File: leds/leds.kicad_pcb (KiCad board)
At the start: 2 copper layers, 230 x 230 mm, 51 parts, among them J101 Conn_02x05_Odd_Even, J102 Conn_02x05_Odd_Even

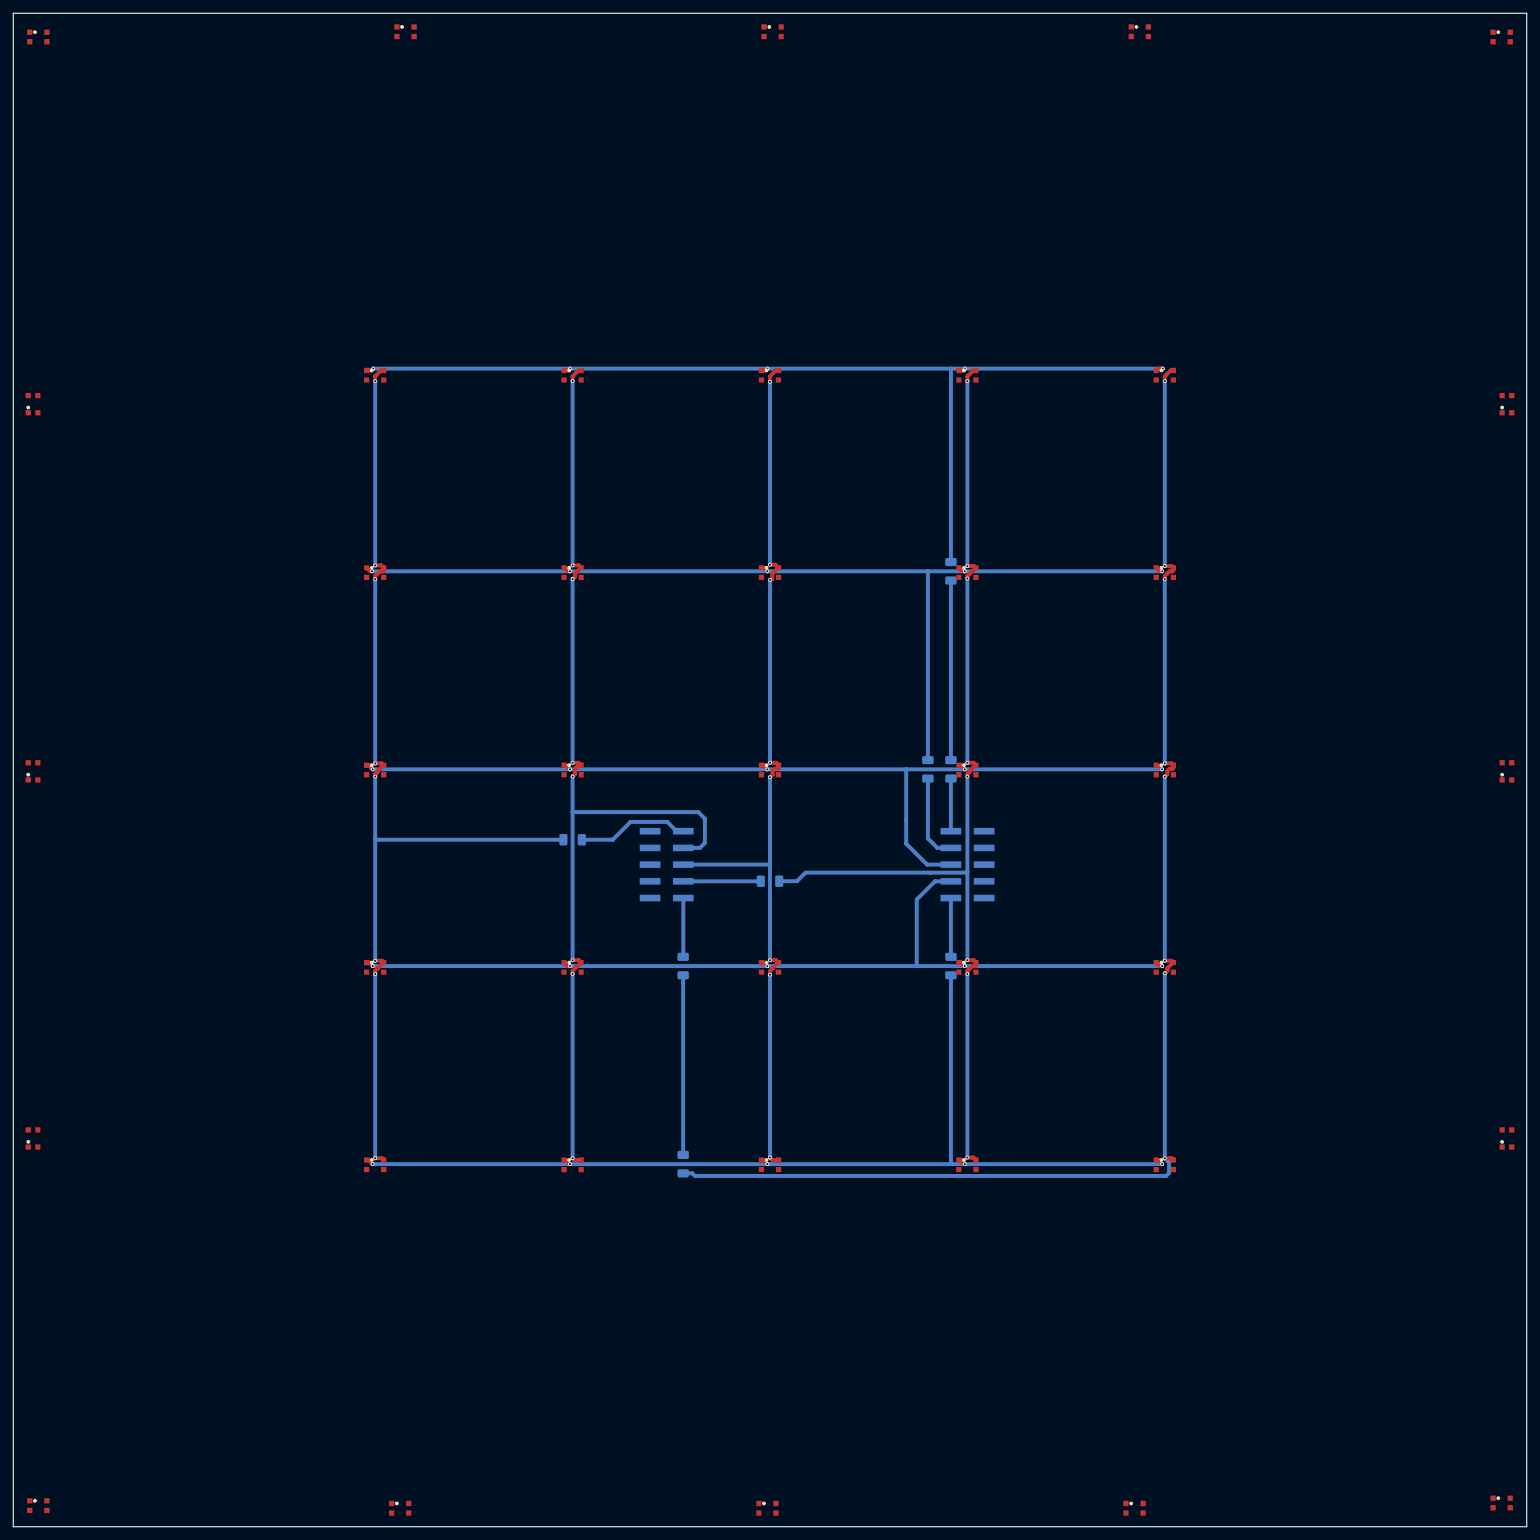
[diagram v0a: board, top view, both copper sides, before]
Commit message: remove unused LEDs, add paste in gerber output
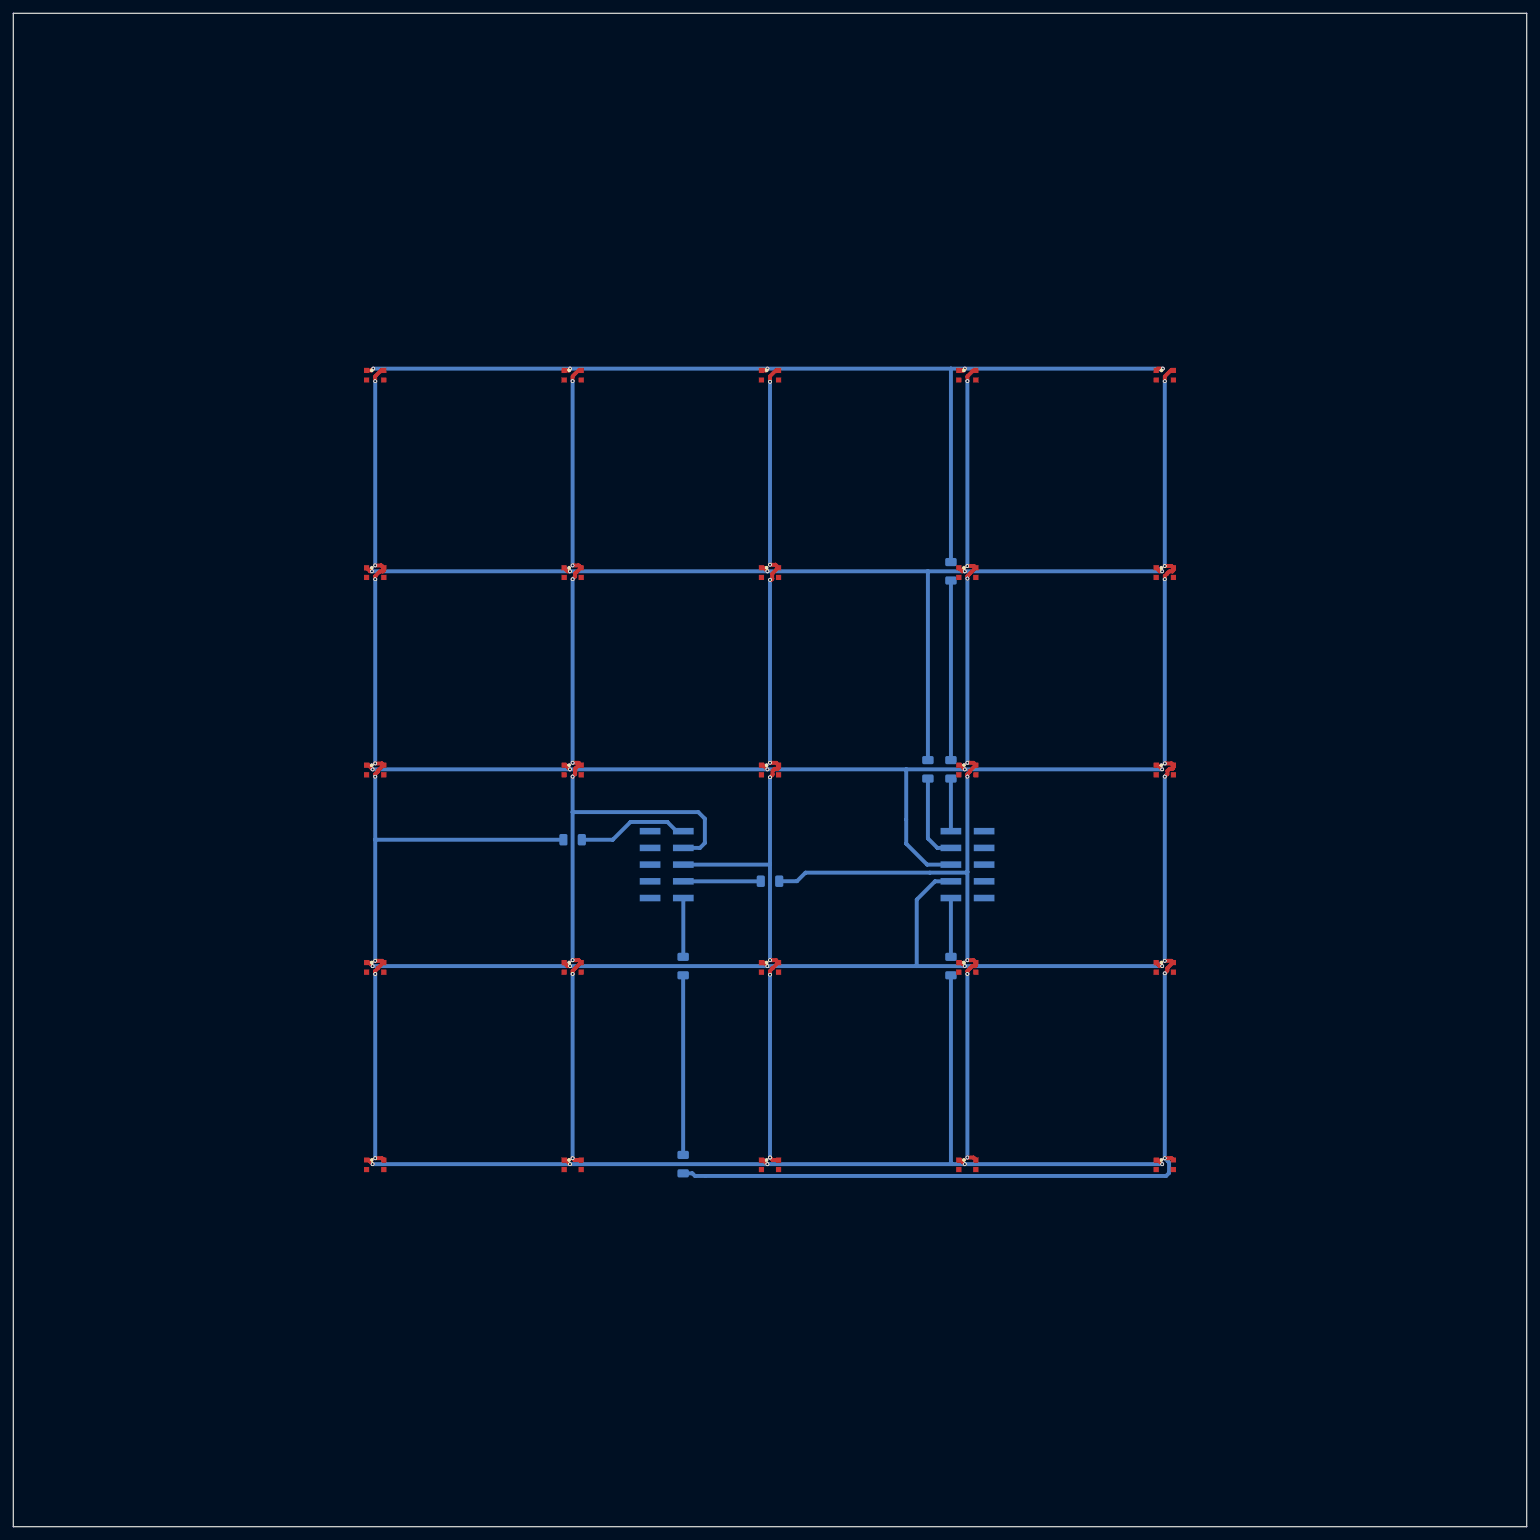
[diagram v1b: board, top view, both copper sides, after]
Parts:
- removed D126, D127, D128, D129, D130, D131, D132, D133, D134, D135, D136, D137, D138, D139, D140, D141: LED_Dual_AACC, leds:Wuerth_150141RV73100
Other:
- net class Default removed
